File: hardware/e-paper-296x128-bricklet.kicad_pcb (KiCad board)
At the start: 2 copper layers, 100 x 40 mm, 37 parts, among them P1 CON-SENSOR, P4 BOOT, P5 DEBUG, Q1 2N7002P, U1 XMC1404, U2 Con24HT, U4 DRILL, U5 DRILL, U6 DRILL, U7 DRILL

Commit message: pcb design
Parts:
- moved C17 79.3 mm to (156.7, 119.8)
- moved C2 79.3 mm to (162.3, 116.8)
- moved D2 79.3 mm to (144.1, 118.2)
- moved D4 79.3 mm to (152.5, 116.9)
- moved C5 79.3 mm to (164.3, 114.3)
- moved D3 79.3 mm to (144.1, 119.8)
- moved L2 79.3 mm to (167.2, 113.0)
- moved Q1 69.4 mm to (166.4, 94.9), turned to 90 degrees
- moved R1 62.2 mm to (161.8, 95.9), turned to 180 degrees
- moved C9 54.5 mm to (164.4, 91.6)
- moved L1 54.2 mm to (169.1, 90.5), turned to 90 degrees
- moved P4 20.3 mm to (142.9, 97.5), turned to 180 degrees
- moved P5 18.0 mm to (140.0, 97.5)
- moved C14 6.82 mm to (127.7, 99.5), turned to 225 degrees
- moved C6 6.46 mm to (126.5, 108.0), turned to 45 degrees
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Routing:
- net VCI: track 0.00 -> 69.1 mm, vias 0 -> 2
- net GND: track 0.00 -> 11.6 mm
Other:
- rule via_min_drill: 0.3 -> 0.2

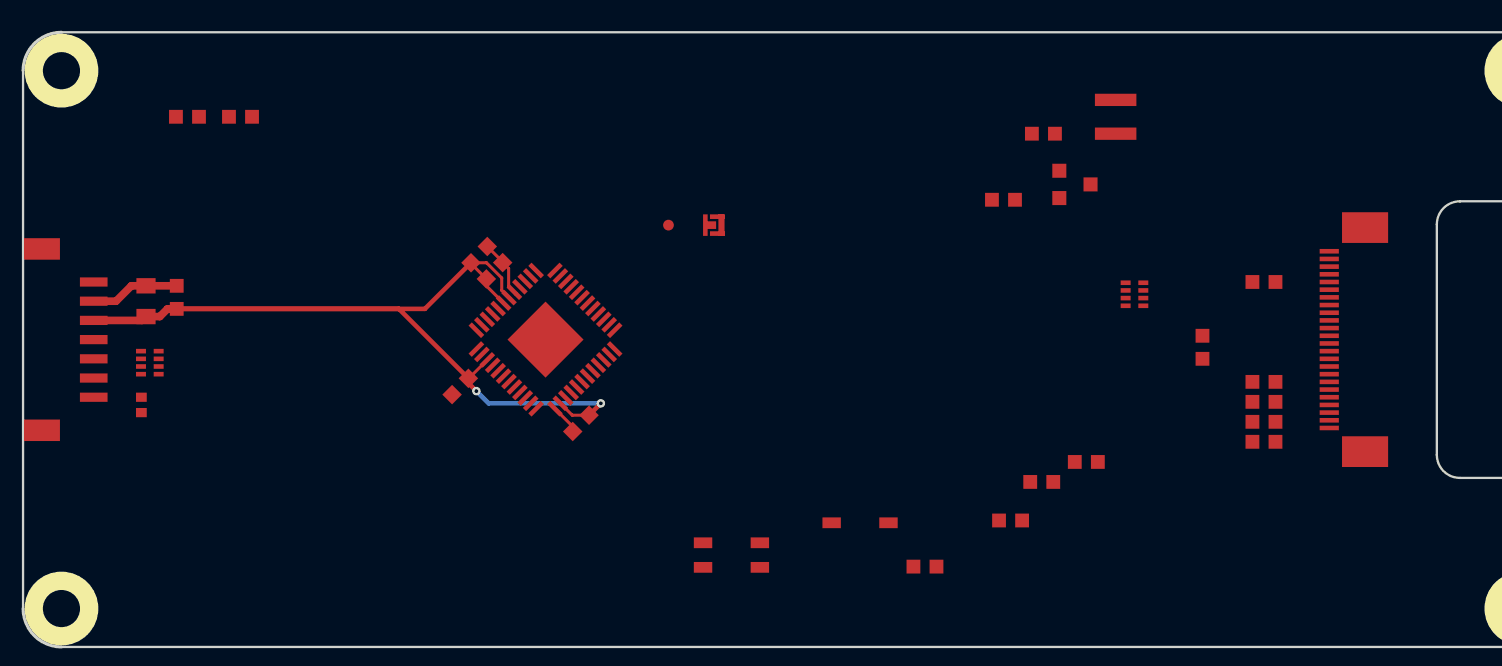
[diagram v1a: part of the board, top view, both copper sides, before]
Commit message: change pcb an schematic design
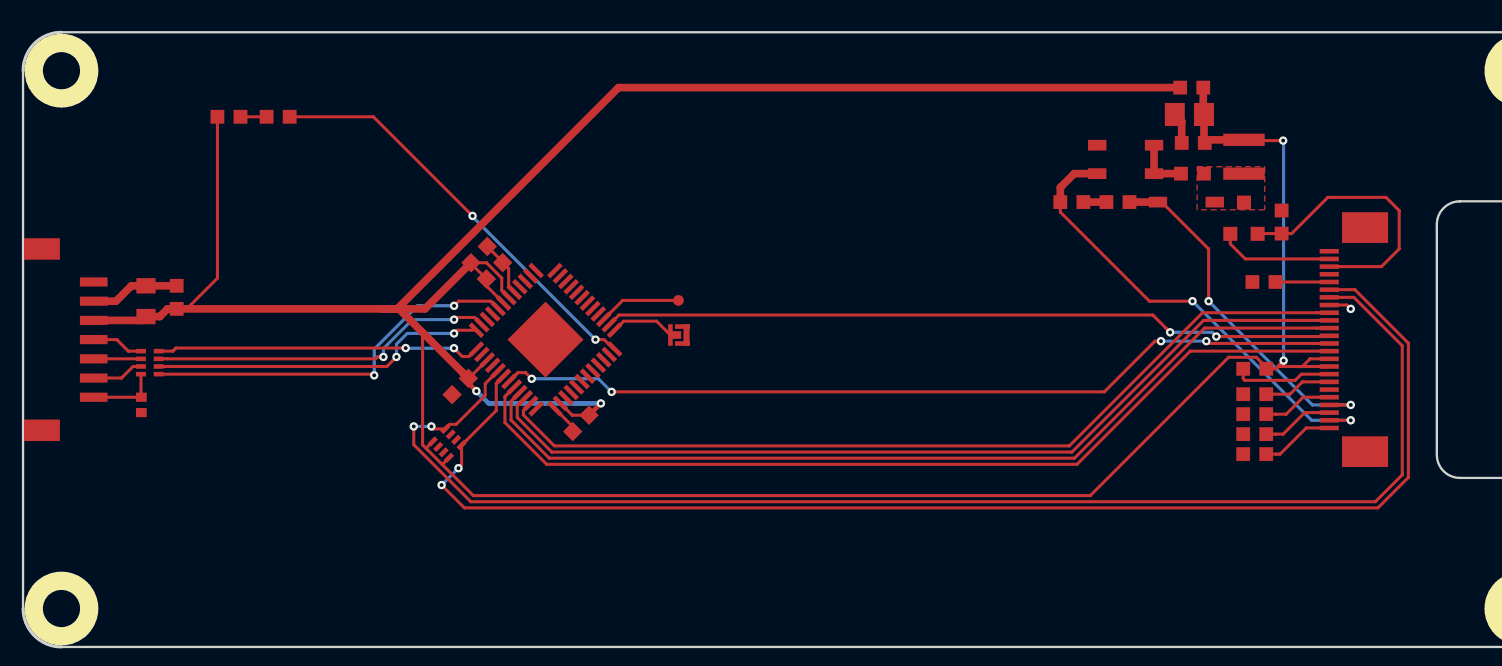
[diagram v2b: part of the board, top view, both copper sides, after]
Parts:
- added C18: 10uF, kicad-libraries:C0805E, F.Cu at (173.9, 90.3)
- moved RP2 45.8 mm to (125.6, 111.8), turned to 315 degrees
- moved D3 38.0 mm to (173.7, 96.0), turned to 180 degrees
- moved D2 35.1 mm to (169.8, 94.2)
- moved C17 32.6 mm to (174.2, 92.2), turned to 180 degrees
- moved D4 30.0 mm to (169.8, 92.3), turned to 180 degrees
- moved L2 25.3 mm to (174.1, 88.6)
- moved C2 21.9 mm to (169.2, 96.0)
- moved C5 18.3 mm to (166.2, 96.0), turned to 180 degrees
- moved R1 18.2 mm to (179.9, 97.3), turned to 90 degrees
- moved Q1 11.2 mm to (177.4, 97.1), turned to 180 degrees
- moved C9 10.0 mm to (174.1, 94.2)
- moved L1 8.75 mm to (177.4, 93.1)
- moved P4 7.50 mm to (140.7, 104.7)
- moved P5 4.94 mm to (140.7, 102.5)
- moved C8 3.68 mm to (178.2, 106.9), turned to 180 degrees
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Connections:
- net Net-(C9-Pad2) renamed +VSW
- RP2 pad 5: TSDA -> TSCL
- RP2 pad 8: TSCL -> TSDA
- U1 pad 33: BUSY -> DC#
- U1 pad 35: DC# -> BUSY
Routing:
- net VCI: track 69.1 -> 248.3 mm, vias 2 -> 4
- net TSDA: track 0.00 -> 89.8 mm, vias 0 -> 2
- net TSCL: track 0.00 -> 88.4 mm, vias 0 -> 2
- net MISO_MOSI: track 0.00 -> 60.4 mm
- net DC#: track 0.00 -> 59.8 mm
- net RES#: track 0.00 -> 58.8 mm
- net BUSY: track 0.00 -> 57.8 mm
- net CLK: track 0.00 -> 55.6 mm, vias 0 -> 4
- net CS#: track 0.00 -> 47.7 mm, vias 0 -> 2
- net VGL: track 0.00 -> 30.3 mm, vias 0 -> 2
- net Net-(R2-Pad1): track 0.00 -> 27.4 mm, vias 0 -> 2
- net S-MISO: track 0.00 -> 25.3 mm, vias 0 -> 2
- net VGH: track 0.00 -> 23.3 mm, vias 0 -> 2
- net S-CLK: track 0.00 -> 22.7 mm, vias 0 -> 2
- net S-MOSI: track 0.00 -> 22.1 mm, vias 0 -> 2
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- added copper zone on F.Cu, net +VSW
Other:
- rule trace_min: 0.2 -> 0.15

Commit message: changed schematic and pcb design
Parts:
- added G***: LOGO, kicad-libraries:Logo_CoMCU, F.Cu at (155.6, 105.0)
- added G***: Logo_31x31, kicad-libraries:Logo_31x31, B.Cu at (99.5, 103.5)
- added VAL: WEEE_7mm, kicad-libraries:WEEE_7mm, F.Cu at (163.0, 105.0)
- added VAL: CE_5mm, kicad-libraries:CE_5mm, F.Cu at (148.3, 105.0)
- moved C18 3.80 mm to (177.4, 89.0)
- moved C17 3.65 mm to (177.4, 90.7)
- moved L2 3.62 mm to (177.4, 87.3)
- moved C11 0.60 mm to (178.2, 101.2)
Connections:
- C12 pad 2: VCI -> 3V3
- C13 pad 2: VCI -> 3V3
- C14 pad 2: VCI -> 3V3
- C3 pad 2: VCI -> 3V3
- C4 pad 2: VCI -> 3V3
- C6 pad 2: VCI -> 3V3
- D1 pad 1: VCI -> 3V3
- L2 pad 1: VCI -> 3V3
- P1 pad 3: VCI -> 3V3
- RP2 pad 1: VCI -> 3V3
- RP2 pad 4: VCI -> 3V3
- U1 pad 18: VCI -> 3V3
- U1 pad 19: VCI -> 3V3
- U1 pad 27: VCI -> 3V3
- U1 pad 38: VCI -> 3V3
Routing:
- net VCI: track 248.3 -> 31.9 mm, vias 4 -> 2
- net 3V3: track 0.00 -> 164.7 mm, vias 0 -> 4
- net GND: track 24.2 -> 53.4 mm, vias 1 -> 26
- net TSCL: track 88.4 -> 89.6 mm
- net Net-(C11-Pad1): track 3.50 -> 4.15 mm
- net TSDA: track 89.8 -> 89.4 mm, vias 2 -> 0
- added copper zone on B.Cu, net GND
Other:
- board text added: "E Paper 296x128"
- board text added: "Status"
- board text added: "tinkerforge.com"

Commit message: final prototype design
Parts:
- L2: footprint kicad-libraries:D0603F -> kicad-libraries:R0603F
- moved D1 4.00 mm to (111.4, 86.5)
- moved R2 4.00 mm to (114.6, 86.5)
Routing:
- net TSCL: track 89.6 -> 95.2 mm
- net 3V3: track 164.7 -> 168.7 mm
- net MISO_MOSI: track 60.4 -> 63.8 mm
- net DC#: track 59.8 -> 62.1 mm
- net Net-(R2-Pad1): track 27.4 -> 29.1 mm
- net GND: track 53.4 -> 54.7 mm
- net RES#: track 58.8 -> 60.0 mm
- net TSDA: track 89.4 -> 90.3 mm
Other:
- outline, holes or cut-outs redrawn
- net class Default: clearance 0.2 -> 0.15
- rule trace_clearance: 0.2 -> 0.15
